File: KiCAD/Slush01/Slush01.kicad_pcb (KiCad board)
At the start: 2 copper layers, 34 x 67 mm, 70 parts, among them IC1 ADR440ARMZ, IC10 AD8237ARMZ, IC11 AD8276ARMZ, IC12 AD8603AUJZ-R2, IC13 AD8237ARMZ, IC2 AD8276ARMZ, IC3 AD8603AUJZ-R2, IC4 AD8237ARMZ, IC5 AD8276ARMZ, IC6 AD8603AUJZ-R2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

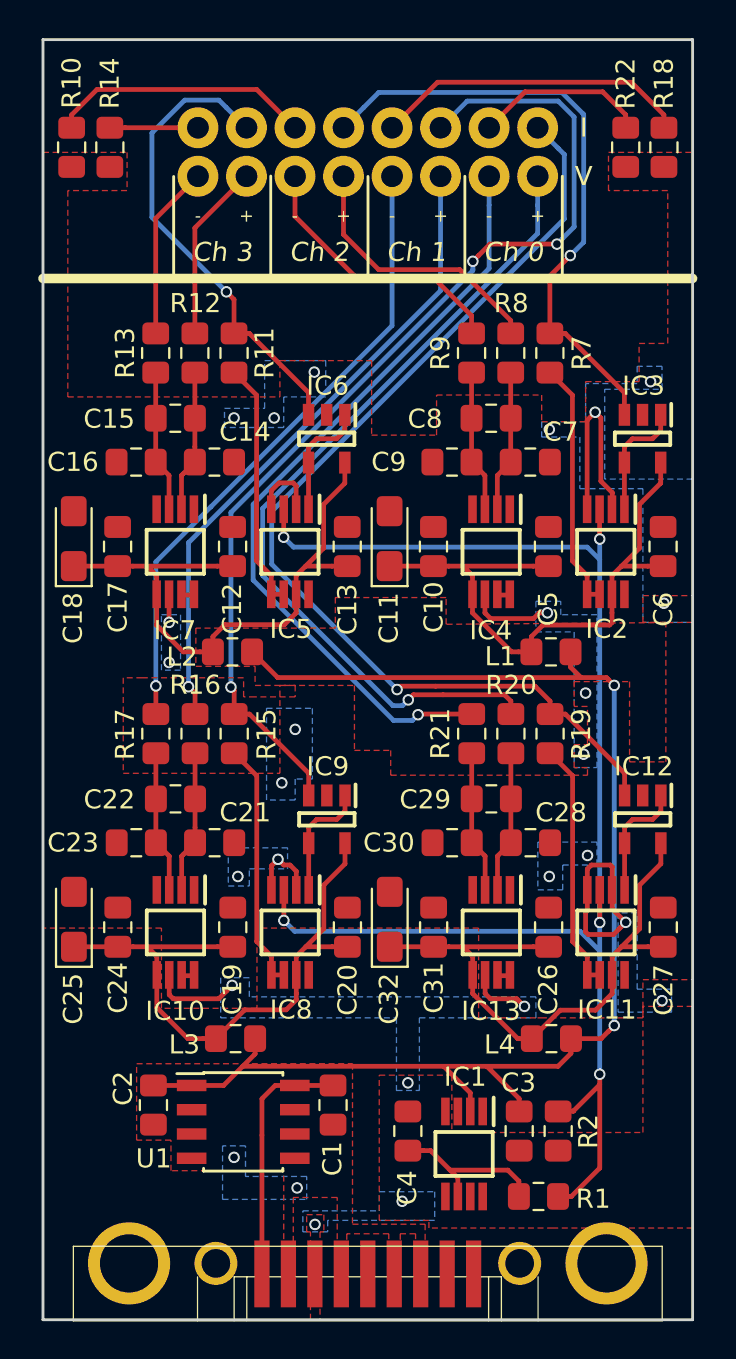
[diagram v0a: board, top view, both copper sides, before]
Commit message: renamed Current_Source to Slush01 and added BOM
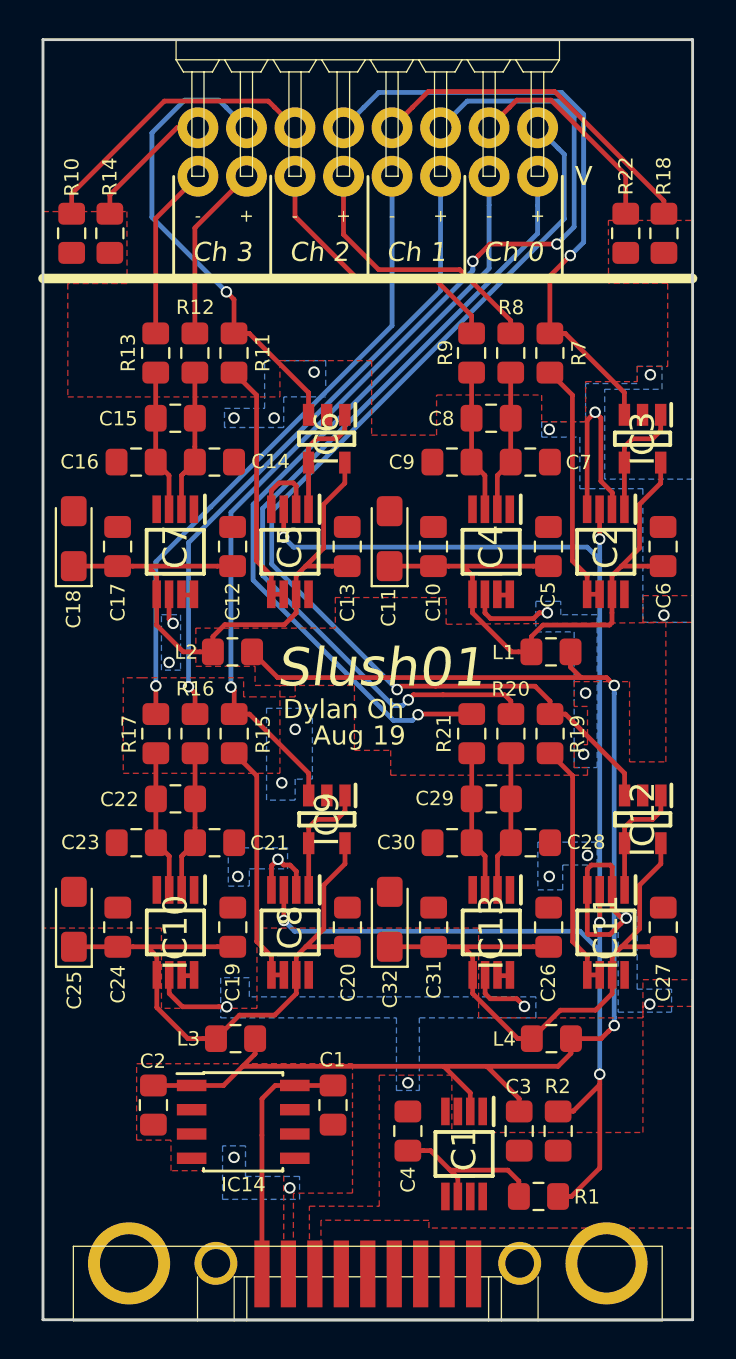
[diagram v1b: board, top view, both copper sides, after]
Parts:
- removed U1: LM78L05_SO8, Package_SO:SOIC-8_3.9x4.9mm_P1.27mm
- added IC14: LM78L05, Slush01:SOIC-8, F.Cu at (63.5, 114.6)
- IC1, IC10, IC11, IC13, IC2, IC4, IC5, IC7, IC8: footprint Current_Source:SOP65P490X110-8N -> Slush01:MSOP-8
- IC12, IC3, IC6, IC9: footprint Current_Source:SOT95P280X100-5N -> Slush01:TSOT-23-5
- J1: footprint Current_Source:K202XHT-E9S-N -> Slush01:K202XHT-E9S-N
- J2: footprint Current_Source:90122-0128 -> Slush01:90122-0128
- moved R10 4.50 mm to (54.5, 68.1)
- moved R14 4.50 mm to (56.5, 68.1)
- moved R18 4.50 mm to (85.5, 68.1)
- moved R22 4.50 mm to (83.5, 68.1)
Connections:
- J1 pad 10: (no net) -> Net-(J1-Pad10)
- J1 pad 4: GND -> (no net)
- J1 pad 7: GND -> (no net)
- J1 pad 8: GND -> (no net)
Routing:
- net /Channel3/I-: track 4.61 -> 7.05 mm
- net /Channel0/I-: track 9.10 -> 11.4 mm
- net /Channel2/I-: track 13.7 -> 15.3 mm
- net /Channel1/I-: track 16.6 -> 18.1 mm
- net GNDA: track 42.7 -> 42.4 mm, vias 25 -> 23
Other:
- board text added: "Aug 19"
- board text added: "Dylan Oh"
- board text added: "Slush01"
